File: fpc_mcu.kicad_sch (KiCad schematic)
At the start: 31 parts, among them J1 USB_B_Micro, SW1 SW_Push, SW2 SW_Push, U1 RP2350_60QFN, U3 W25Q128JVS, U7 SiT2001B

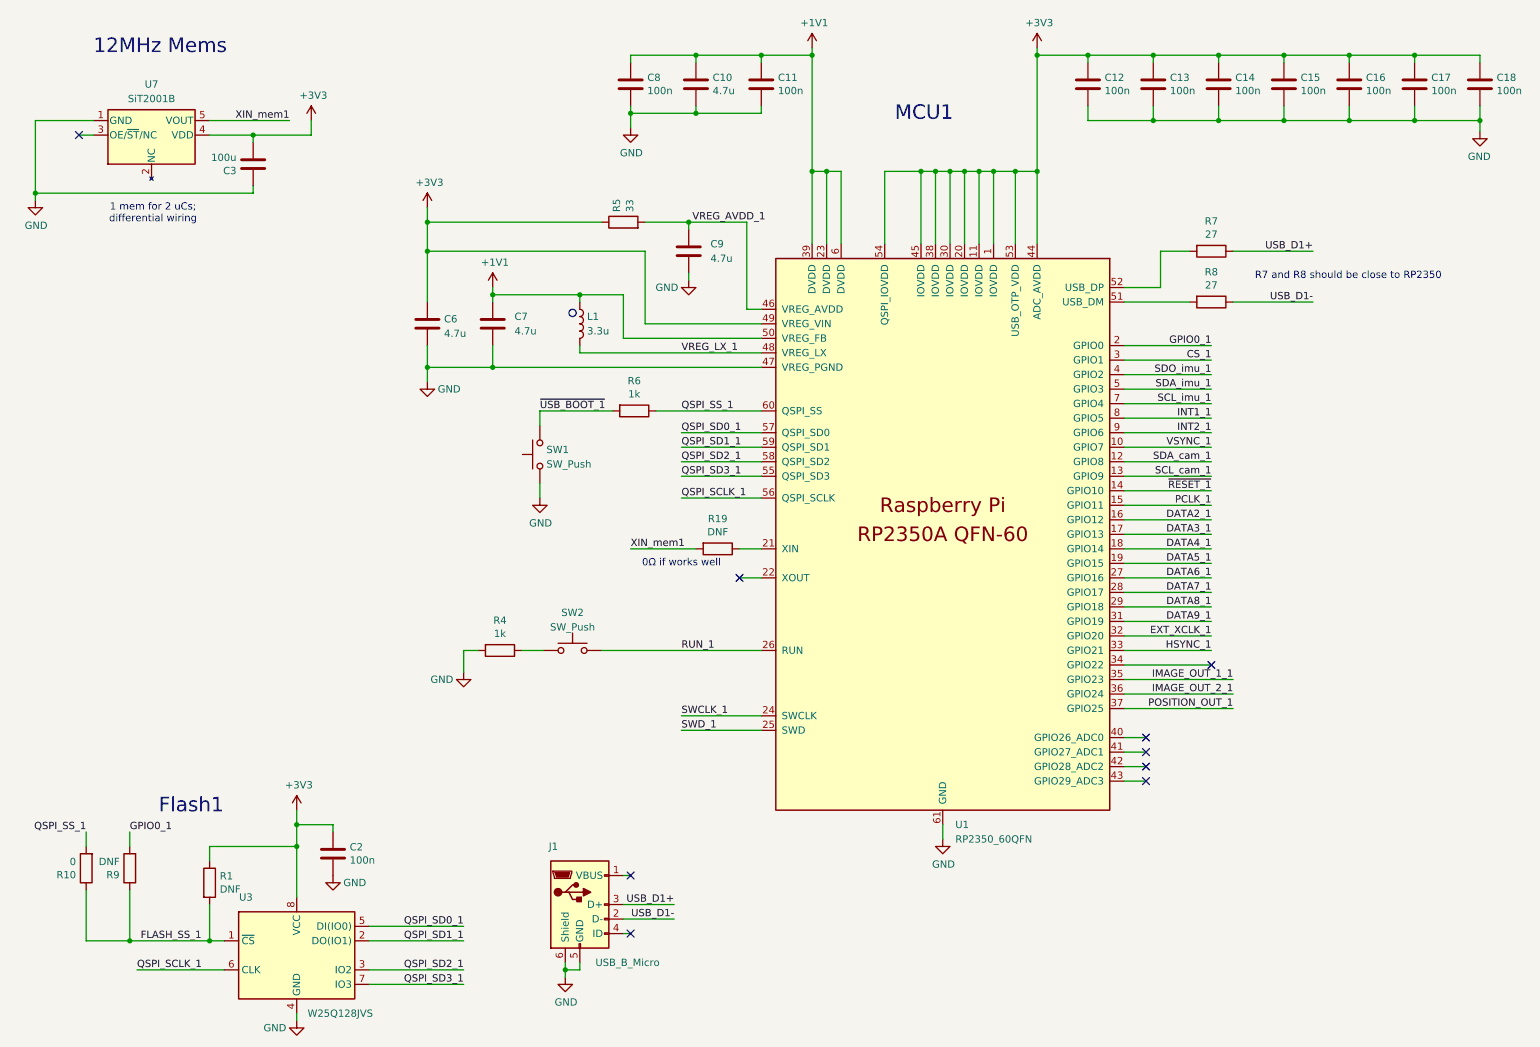
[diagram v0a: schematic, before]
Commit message: discarded 24MHz crystal. ERC passed 1st time
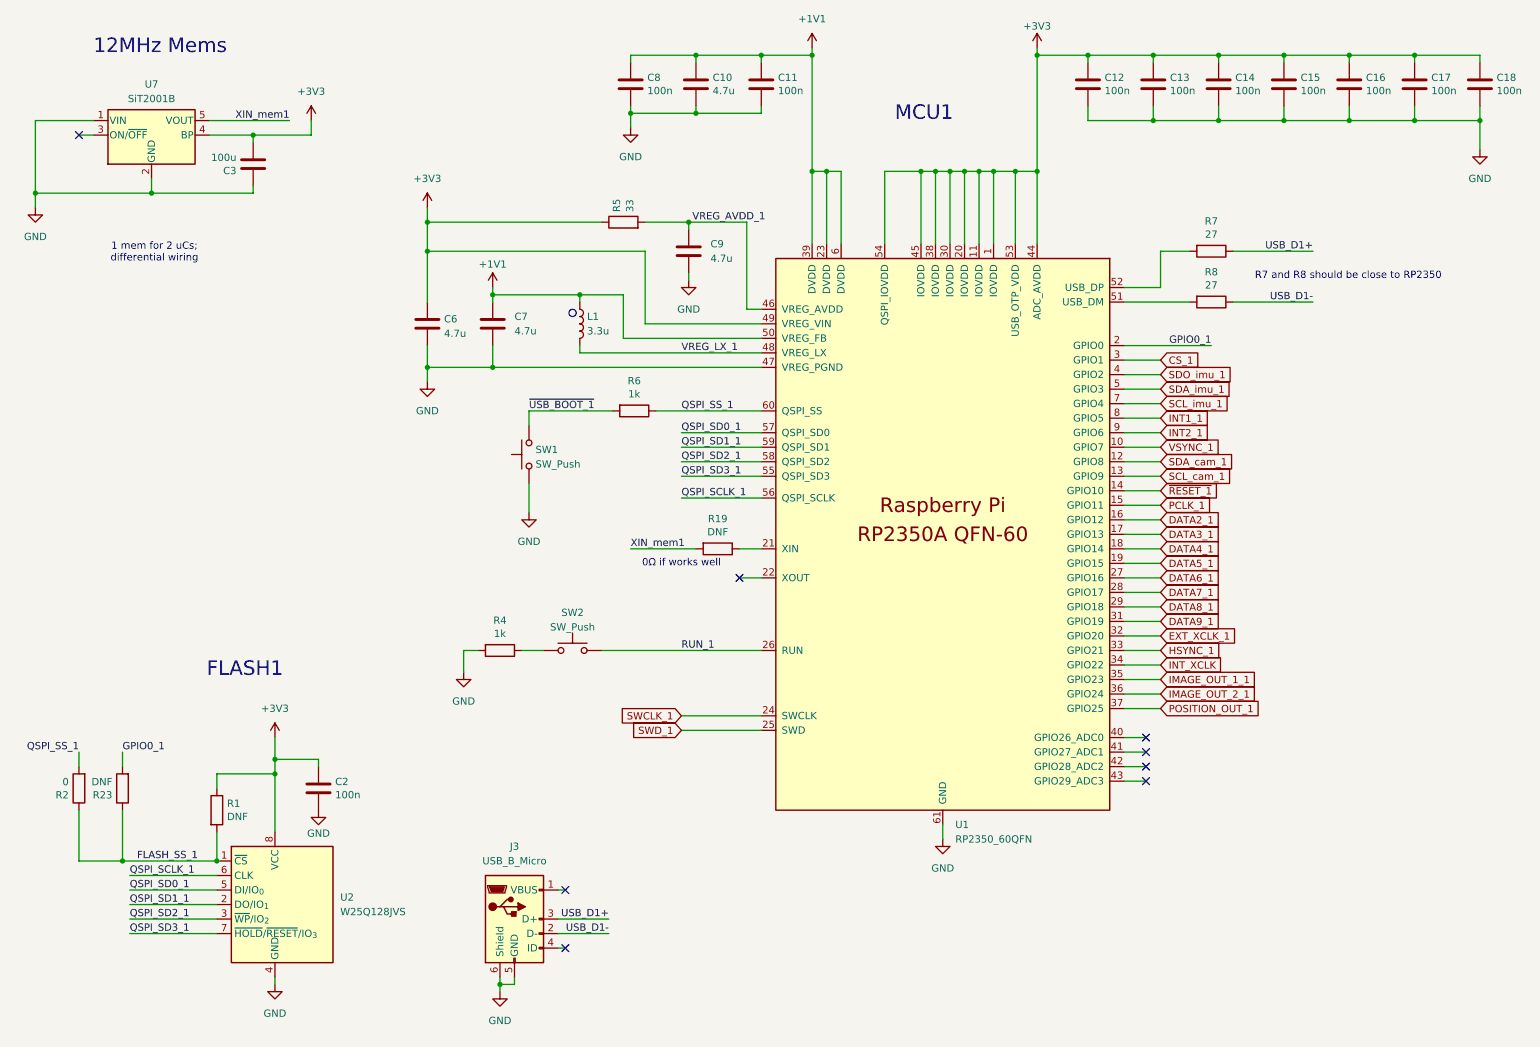
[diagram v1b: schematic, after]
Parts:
- removed J1: USB_B_Micro, Connector_USB:USB_Micro-B_Amphenol_10103594-0001LF_Horizontal, symbol Connector:USB_B_Micro
- removed R10: 0, Resistor_SMD:R_0603_1608Metric_Pad0.98x0.95mm_HandSolder, symbol Device:R
- removed R9: DNF, Resistor_SMD:R_0603_1608Metric_Pad0.98x0.95mm_HandSolder, symbol Device:R
- removed U3: W25Q128JVS, Package_SO:SOIC-8_5.23x5.23mm_P1.27mm, symbol Memory_Flash:W25Q128JVS
- added J3: USB_B_Micro, symbol Connector:USB_B_Micro
- added R2: 0, Resistor_SMD:R_0603_1608Metric_Pad0.98x0.95mm_HandSolder, symbol Device:R
- added R23: DNF, Resistor_SMD:R_0603_1608Metric_Pad0.98x0.95mm_HandSolder, symbol Device:R
- added U2: W25Q128JVS, Package_SO:SOIC-8_5.3x5.3mm_P1.27mm, symbol Memory_Flash:W25Q128JVS
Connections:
- net +3V3: now also U2.8 (VCC)
- net FLASH_SS_1: now also R2.1, R23.1, U2.1 (~{CS})
- net GND: now also U7.2 (GND), J3.5 (GND), J3.6 (Shield), U2.4 (GND)
- net GPIO0_1: now also R23.2
- net QSPI_SCLK_1: now also U2.6 (CLK)
- net QSPI_SD0_1: now also U2.5 (DI/IO_{0})
- net QSPI_SD1_1: now also U2.2 (DO/IO_{1})
- net QSPI_SD2_1: now also U2.3 (~{WP}/IO_{2})
- net QSPI_SD3_1: now also U2.7 (~{HOLD}/~{RESET}/IO_{3})
- net QSPI_SS_1: now also R2.2
- net USB_D1+: now also J3.3 (D+)
- net USB_D1-: now also J3.2 (D-)
- net INT_XCLK: now reaches U1.34 (GPIO22)
- no-connect marks 9 -> 8
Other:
- note added: "FLASH1"
- note removed: "Flash1"
- moved on the sheet: C2, R1, SW1

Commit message: updates in layout
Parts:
- added TP2: TestPoint, TestPoint:TestPoint_Pad_D1.0mm, symbol Connector:TestPoint
- J3: footprint (none) -> RP2350_60QFN_minimal:USB_Micro-B_Amphenol_10103594-0001LF_Horizontal_modified
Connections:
- net +1V1: now also TP2.1
- net +3V3 renamed +3.3V

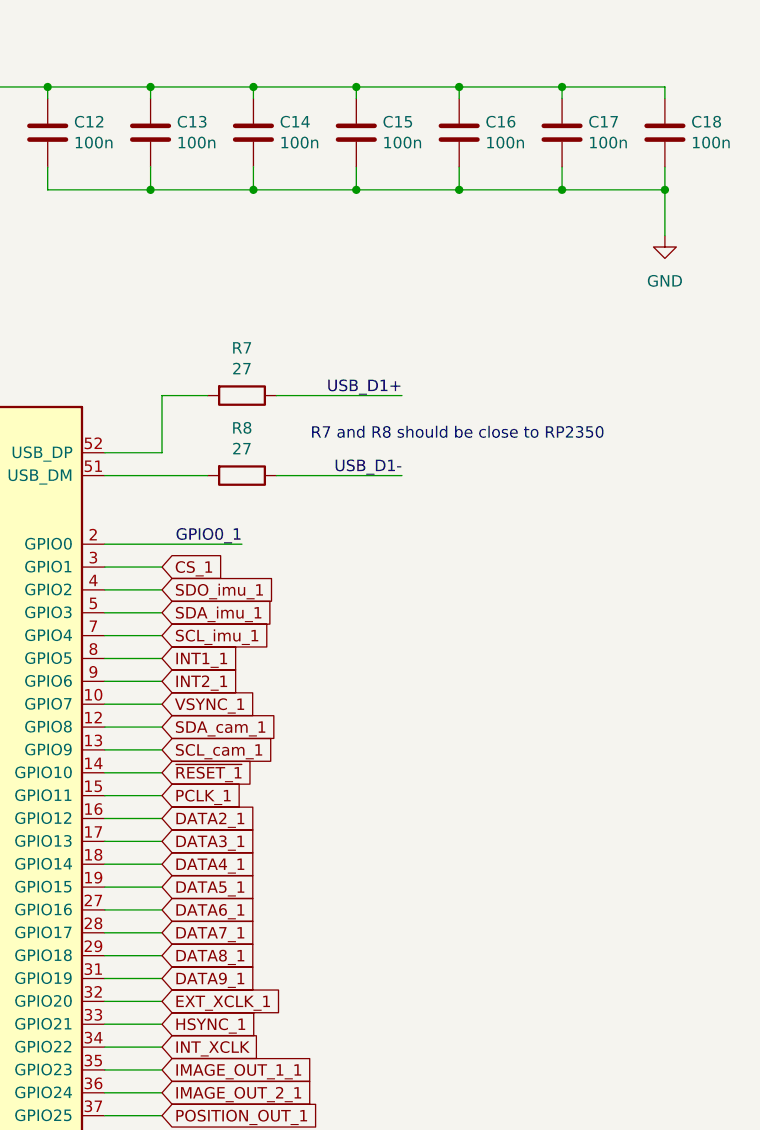
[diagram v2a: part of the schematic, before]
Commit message: vital change to pin order of connector; RP2350 SMPS layout changed
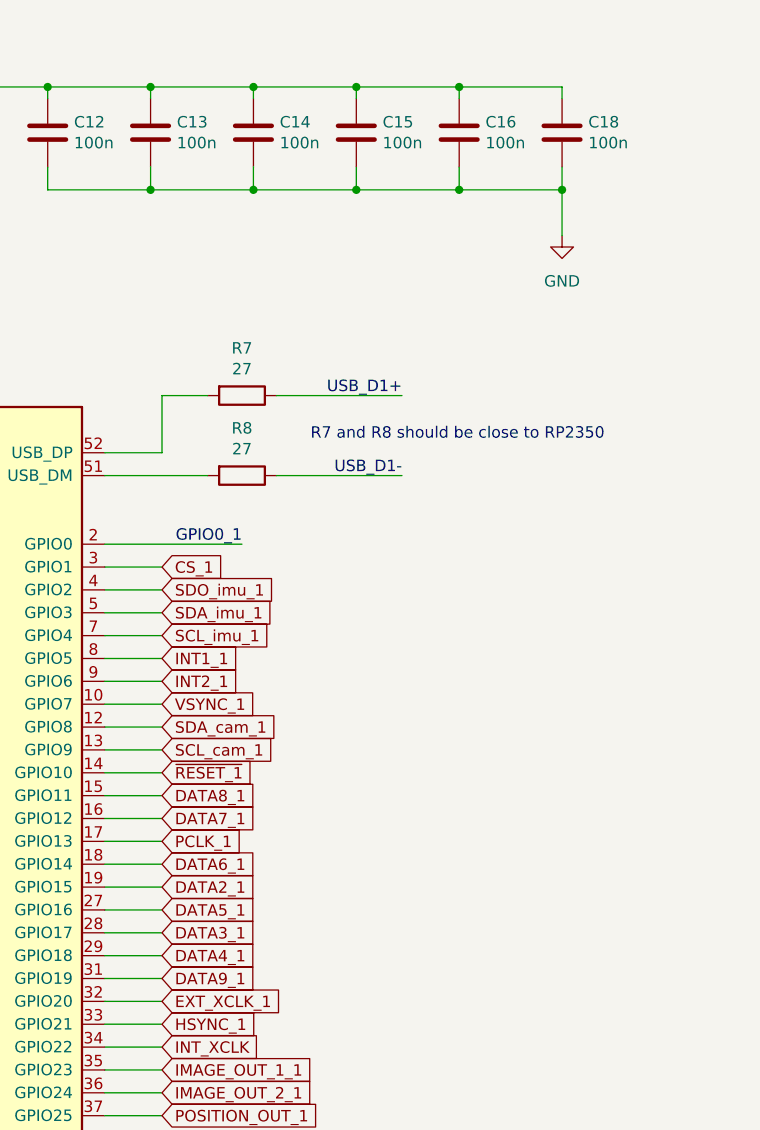
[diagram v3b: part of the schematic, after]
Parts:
- removed C17: 100n, Capacitor_SMD:C_0603_1608Metric_Pad1.08x0.95mm_HandSolder, symbol Device:C
- L1: footprint Inductor_SMD:L_0603_1608Metric_Pad1.05x0.95mm_HandSolder -> RP2350_60QFN_minimal:L_pol_2016
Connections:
- net DATA2_1: now also U1.19 (GPIO15); no longer U1.16 (GPIO12)
- net DATA3_1: now also U1.28 (GPIO17); no longer U1.17 (GPIO13)
- net DATA4_1: now also U1.29 (GPIO18); no longer U1.18 (GPIO14)
- net DATA5_1: now also U1.27 (GPIO16); no longer U1.19 (GPIO15)
- net DATA6_1: now also U1.18 (GPIO14); no longer U1.27 (GPIO16)
- net DATA7_1: now also U1.16 (GPIO12); no longer U1.28 (GPIO17)
- net DATA8_1: now also U1.15 (GPIO11); no longer U1.29 (GPIO18)
- net PCLK_1: now also U1.17 (GPIO13); no longer U1.15 (GPIO11)
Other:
- moved on the sheet: C18
